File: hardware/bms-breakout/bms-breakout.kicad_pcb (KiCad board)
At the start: 2 copper layers, 150.2 x 100 mm, 26 parts, among them J1 IN-A, J10 V-SUPP, J11 Smol_Brain_Board, J13 UART_CONN, J16 ESTOP_CON, J17 I2C_Conn, J18 BAL_3, J19 BAL_2, J2 IN-B, J20 BAL_1, J21 DE9_Socket_MountingHoles, J22 DE9_Socket_MountingHoles, J23 FAN-IN, J24 SWITCH, J3 IN-C, J4 BALANCE-A, J5 BALANCE-B, J6 BALANCE-C, J7 Conn_01x02, J8 BMS-OUT, J9 BMS-IN, Q1 PMOZZ, SW1 SW_DIP_x02

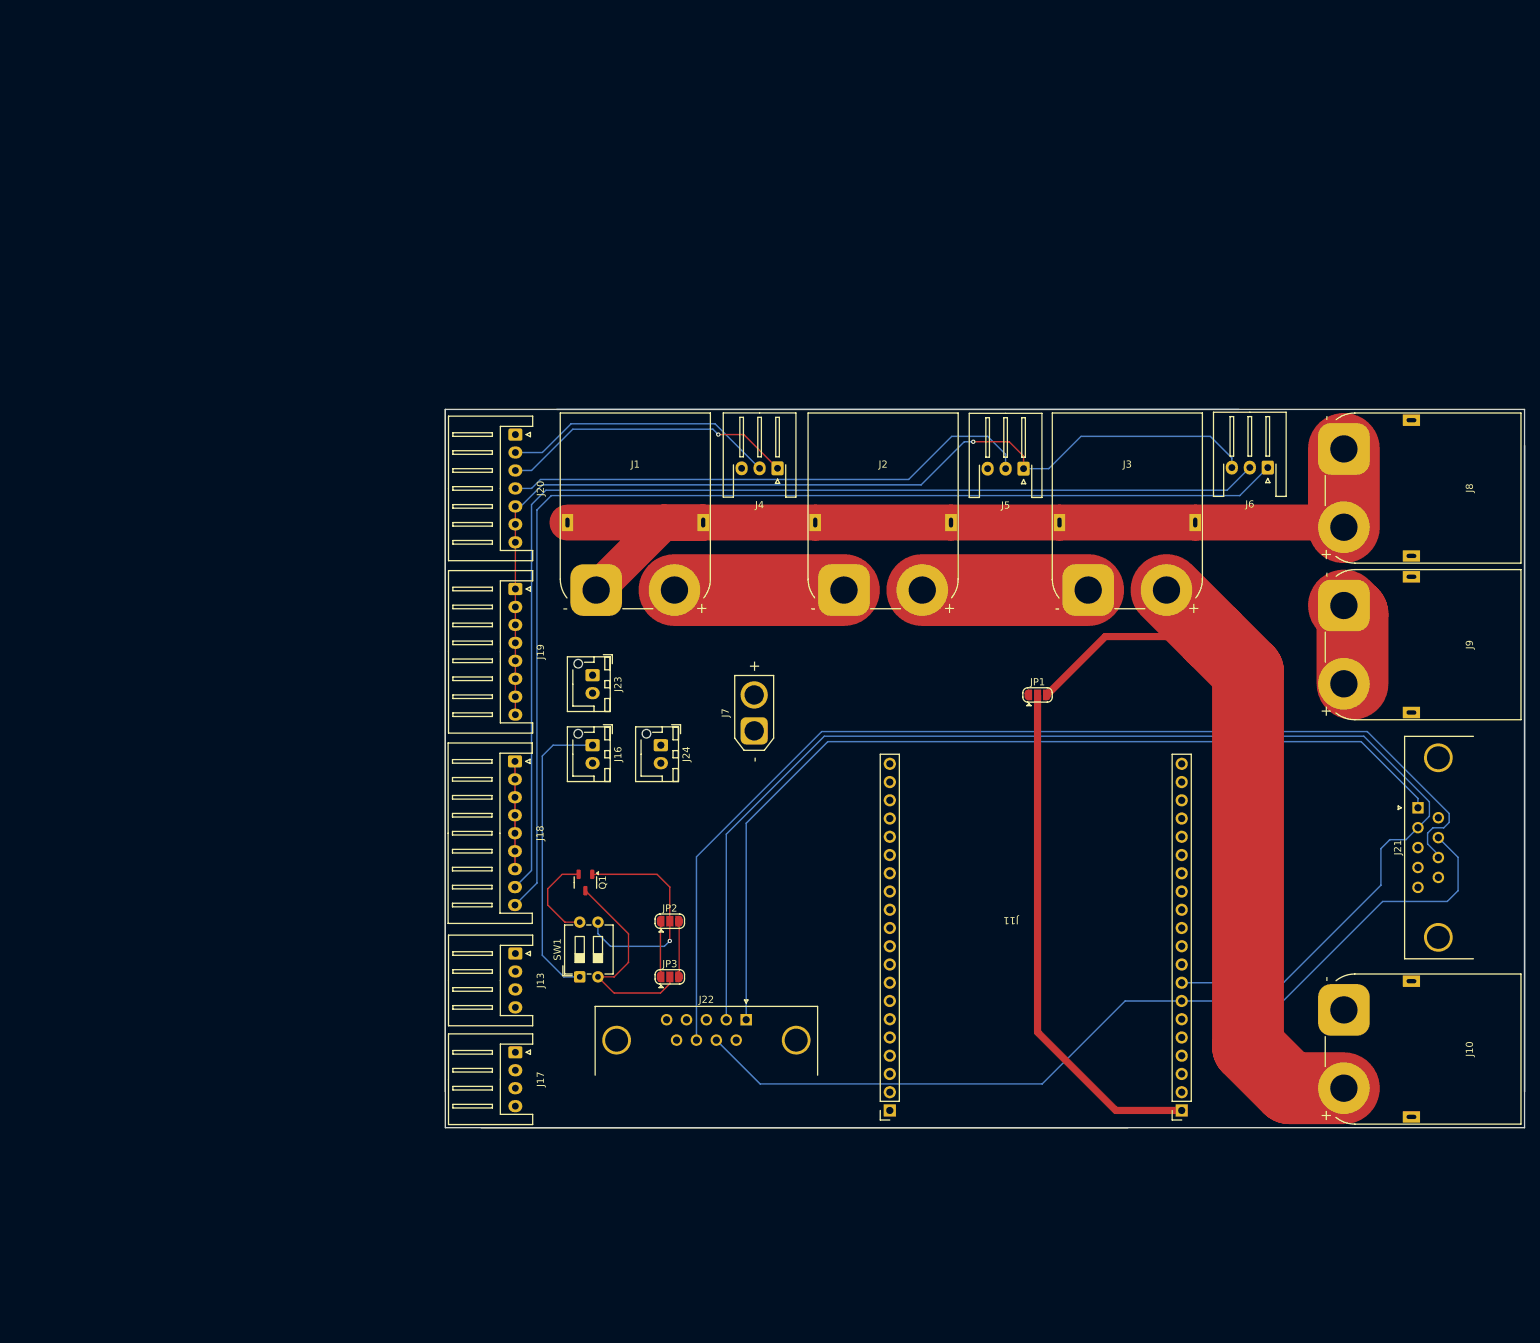
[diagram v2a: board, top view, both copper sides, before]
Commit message: Redid layout
- Redid layout
- Currently tracing board
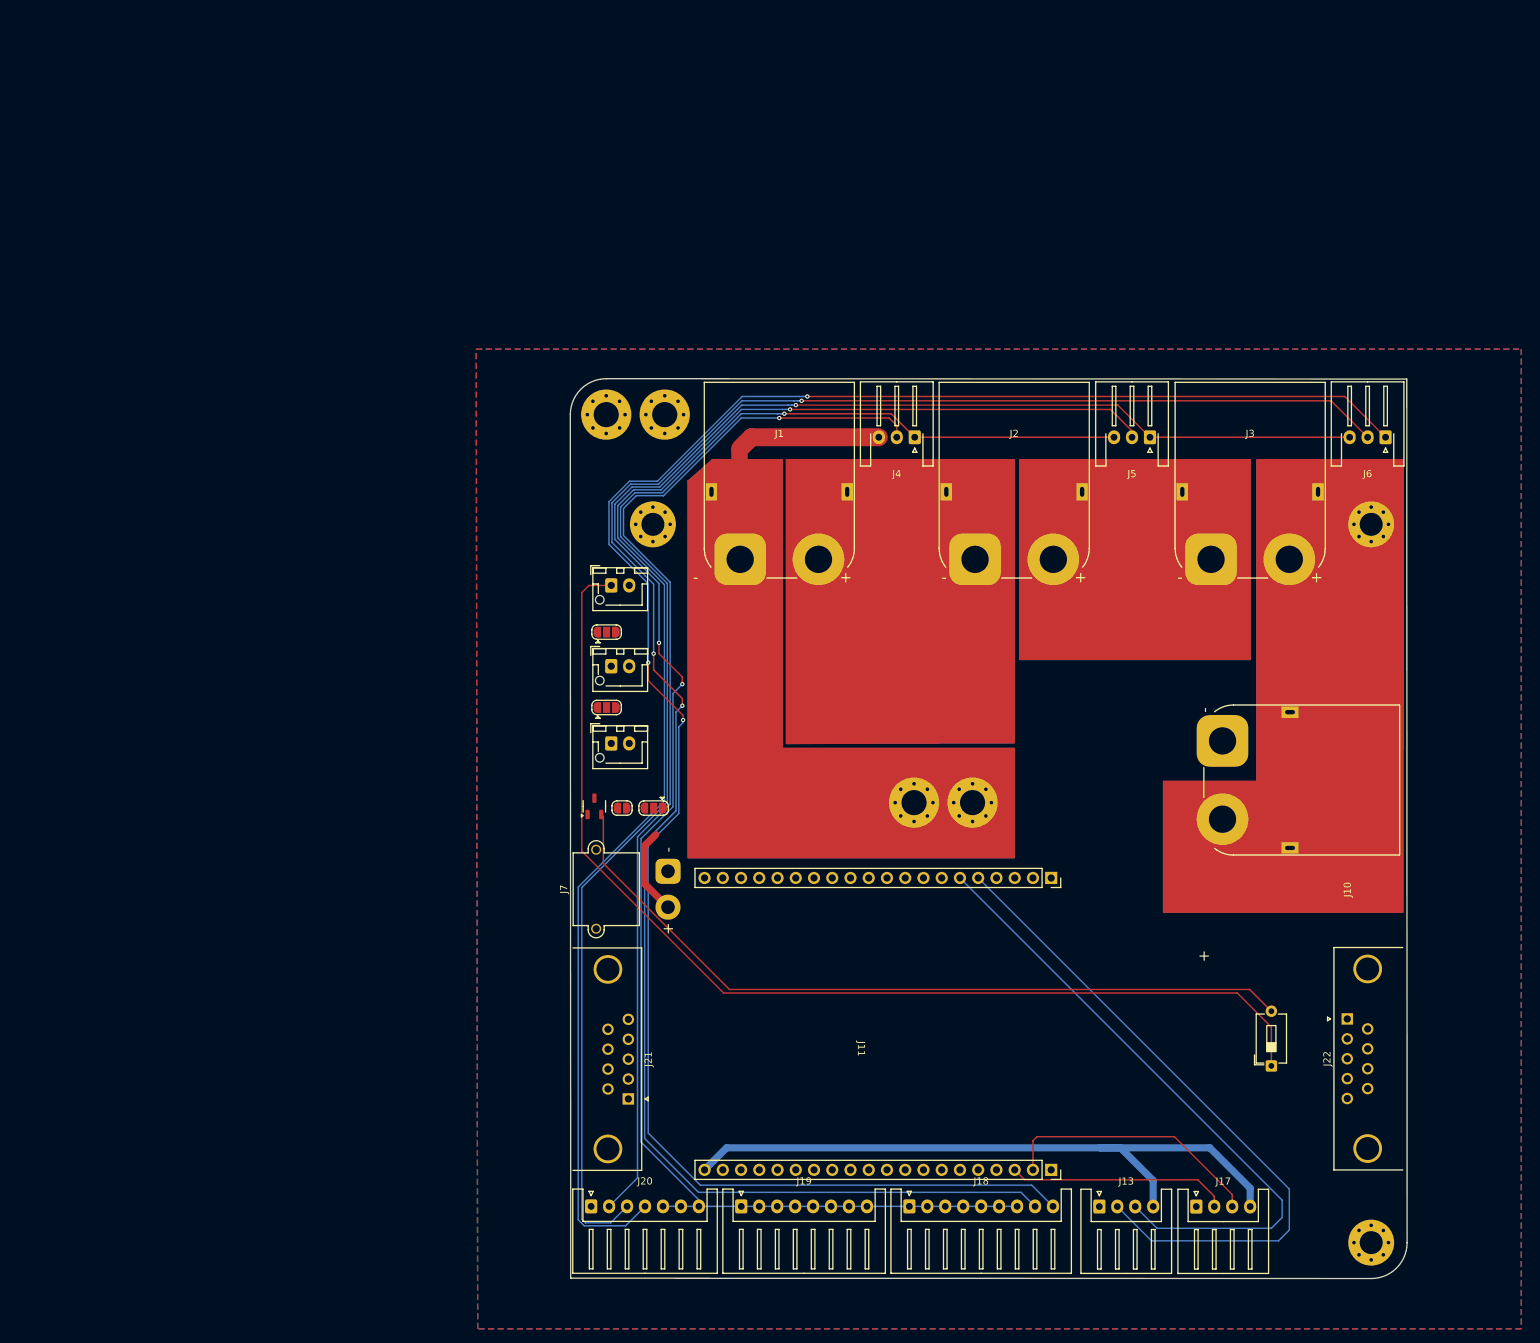
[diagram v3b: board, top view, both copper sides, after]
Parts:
- removed J8: BMS-OUT, Connector_AMASS:AMASS_XT90PW-M_1x02_P10.90mm_Horizontal
- removed J9: BMS-IN, Connector_AMASS:AMASS_XT90PW-M_1x02_P10.90mm_Horizontal
- removed SW1: SW_DIP_x02, Button_Switch_THT:SW_DIP_SPSTx02_Slide_6.7x6.64mm_W7.62mm_P2.54mm_LowProfile
- added H1: Mounting_1, MountingHole:MountingHole_3.2mm_M3_Pad_Via, F.Cu at (78.9, 61.0)
- added H2: Mounting_2, MountingHole:MountingHole_3.2mm_M3_Pad_Via, F.Cu at (178.9, 161.0)
- added H3: Mounting_3, MountingHole:MountingHole_3.2mm_M3_Pad_Via, F.Cu at (178.9, 61.0)
- added H5: BMS_OUT, MountingHole:MountingHole_3.5mm_Pad_Via, F.Cu at (72.4, 45.7)
- added H6: BMS_OUT, MountingHole:MountingHole_3.5mm_Pad_Via, F.Cu at (80.5, 45.7)
- added H7: BMS_IN, MountingHole:MountingHole_3.5mm_Pad_Via, F.Cu at (115.3, 99.7)
- added H8: BMS_IN, MountingHole:MountingHole_3.5mm_Pad_Via, F.Cu at (123.4, 99.7)
- added JP4: Mozz_Jumper, Jumper:SolderJumper-2_P1.3mm_Open_RoundedPad1.0x1.5mm, F.Cu at (74.6, 100.5)
- added SW2: Kill_Switch, Button_Switch_THT:SW_DIP_SPSTx01_Slide_6.7x4.1mm_W7.62mm_P2.54mm_LowProfile, F.Cu at (165.0, 136.4)
- J7: footprint Connector_AMASS:AMASS_XT30U-M_1x02_P5.0mm_Vertical -> Connector_AMASS:AMASS_XT30PW-M_1x02_P2.50mm_Horizontal
- moved J21 117.2 mm to (75.5, 141.0), turned to -90 degrees
- moved J20 108.0 mm to (70.3, 156.0), turned to 0 degrees
- moved J17 97.2 mm to (154.6, 156.0), turned to 0 degrees
- moved J19 91.5 mm to (91.2, 156.0), turned to 0 degrees
- moved J13 88.6 mm to (141.1, 156.0), turned to 0 degrees
- moved J22 83.7 mm to (175.6, 129.9), turned to 90 degrees
- moved J18 82.8 mm to (114.6, 156.0), turned to 0 degrees
- moved JP1 55.7 mm to (79.0, 100.5), turned to 180 degrees
- moved JP2 41.2 mm to (72.5, 76.0)
- moved J10 41.1 mm to (158.2, 91.2)
- moved JP3 38.5 mm to (72.5, 86.5)
- moved J11 28.2 mm to (107.4, 134.0), turned to -90 degrees
- moved J7 22.9 mm to (81.0, 109.3)
- moved J16 22.4 mm to (73.1, 69.5), turned to 0 degrees
- moved J1 20.5 mm to (91.0, 65.9)
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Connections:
- net Net-(J1-Pin_2) renamed /BAT1-2
- net Net-(J2-Pin_2) renamed /BAT2-3
- J1 pad MP: GND_B -> unconnected-(J1-MountPin-PadMP)
- J10 pad MP: GND_C -> unconnected-(J10-MountPin-PadMP)_1
- J2 pad MP: GND_B -> unconnected-(J2-MountPin-PadMP)
- J24 pad 1: /K+ -> /K_NEG
- J24 pad 2: /K+ -> /K_POS
- J3 pad MP: GND_B -> unconnected-(J3-MountPin-PadMP)
- JP2 pad 1: /K+ -> /K_NEG
- JP2 pad 3: /K+ -> /K_POS
- JP3 pad 1: /K+ -> /K_NEG
- JP3 pad 3: /K+ -> /K_POS
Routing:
- net /CAN_L_A: track 182.4 -> 0.00 mm
- net /CAN_H_B: track 151.1 -> 0.00 mm
- net /BAL_2: track 41.1 -> 189.7 mm
- net /CAN_L_B: track 130.2 -> 0.00 mm
- net /CAN_H_A: track 125.5 -> 0.00 mm
- net /BAL_3: track 74.3 -> 197.1 mm, vias 0 -> 1
- net GND_B: track 138.1 -> 20.0 mm
- net /BAL_4: track 154.5 -> 266.5 mm, vias 1 -> 3
- net /BAL_6: track 160.5 -> 271.3 mm, vias 0 -> 3
- net VBUS: track 110.5 -> 0.00 mm
- net /BAL_1: track 38.2 -> 148.7 mm, vias 0 -> 1
- net Net-(J16-Pin_1): track 41.8 -> 152.0 mm
- net /BAL_5: track 156.3 -> 266.2 mm, vias 0 -> 3
- net Net-(Q1-G): track 12.8 -> 108.4 mm
- net +3V3: track 0.00 -> 95.0 mm
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- added copper zone on B.Cu, net GND_C
- added copper zone on F.Cu, net GND_C
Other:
- board size 150.2 x 100 mm -> 116.5 x 125.3 mm

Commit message: Almost finished tracing BMS
- Updated GND planes
- CAN Traces almost done
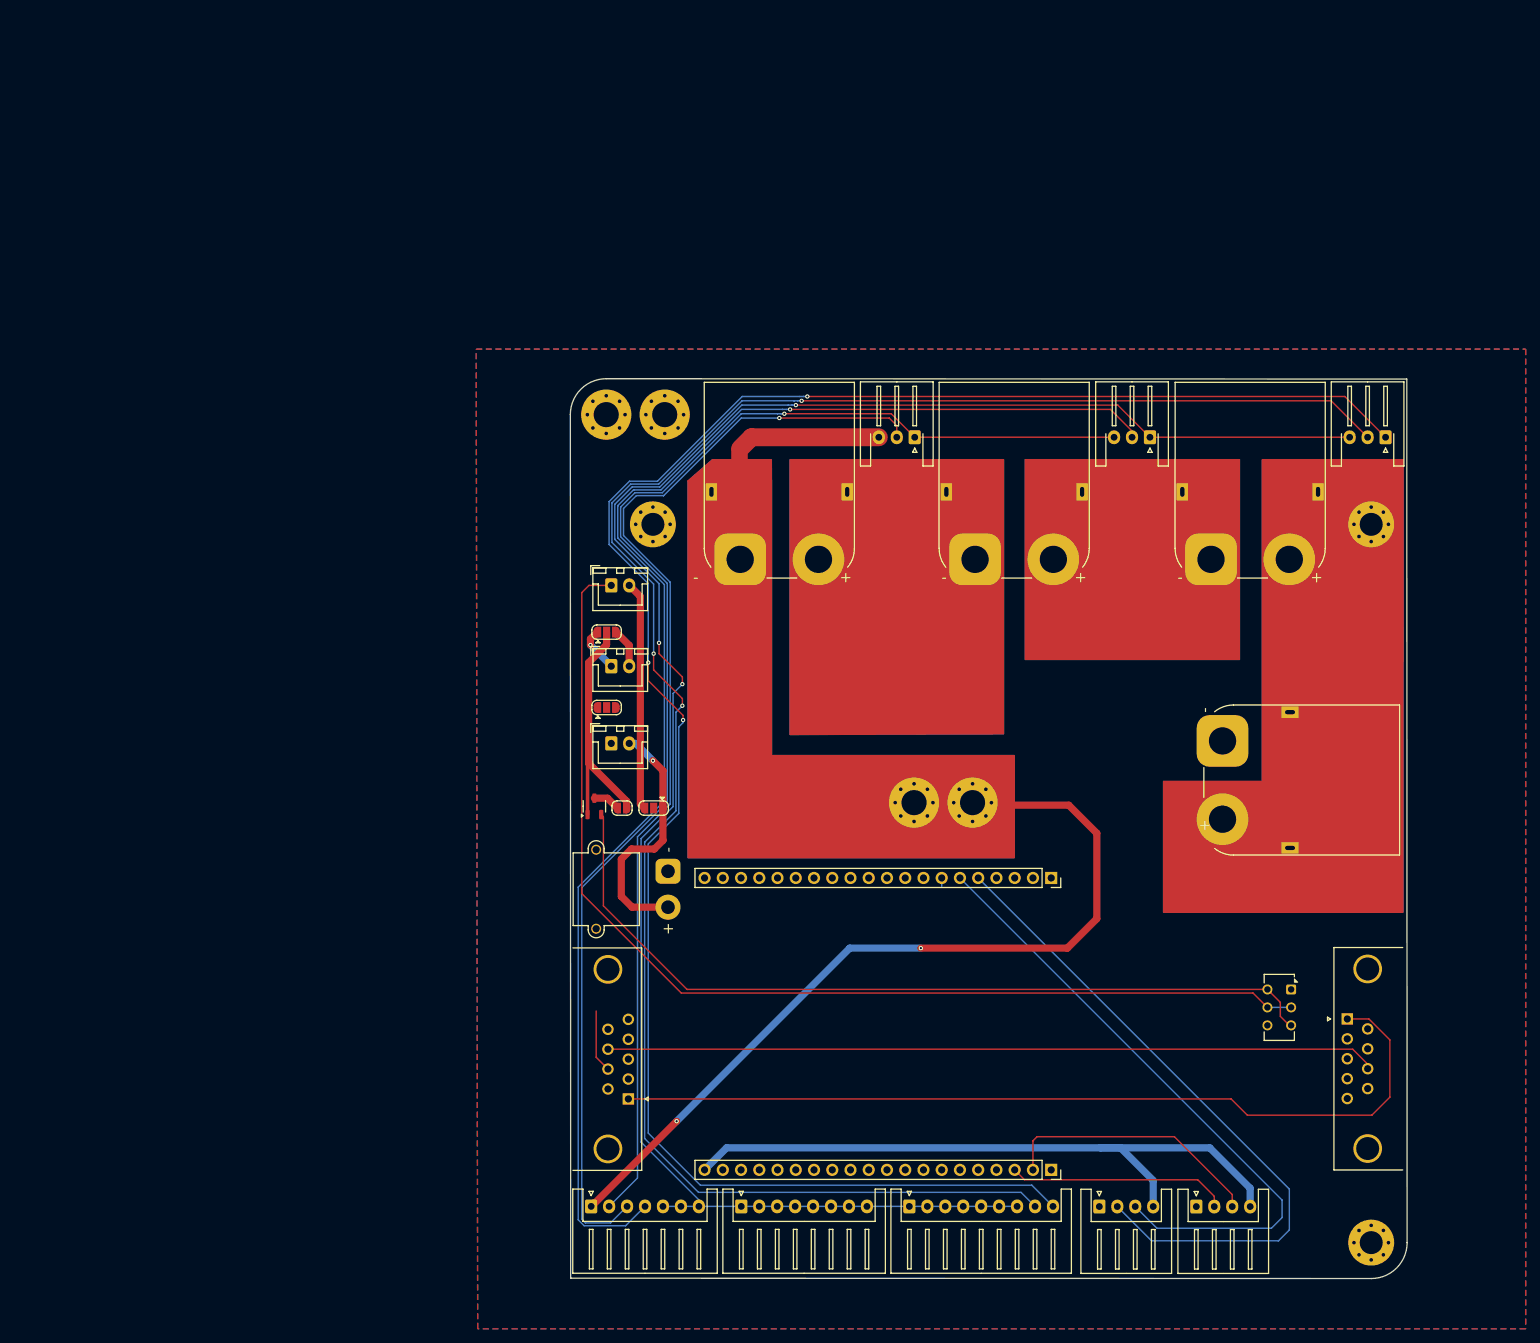
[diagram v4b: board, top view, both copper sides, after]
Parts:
- removed SW2: Kill_Switch, Button_Switch_THT:SW_DIP_SPSTx01_Slide_6.7x4.1mm_W7.62mm_P2.54mm_LowProfile
- added SW1: Kill_Switch, Button_Switch_THT:SW_CK_JS202011CQN_DPDT_Straight, F.Cu at (167.8, 125.8)
- J16, J23, J24: footprint Connector_JST:JST_XH_B2B-XH-AM_1x02_P2.50mm_Vertical -> Connector_JST:JST_XH_B2B-XH-A_1x02_P2.50mm_Vertical
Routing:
- net /CAN_L_B: track 0.00 -> 123.1 mm
- net GND_B: track 20.0 -> 137.9 mm, vias 0 -> 2
- net /CAN_H_B: track 0.00 -> 107.3 mm
- net Net-(JP2-C): track 0.00 -> 34.9 mm
- net VBUS: track 0.00 -> 31.9 mm
- net VCC: track 12.1 -> 35.2 mm, vias 0 -> 1
- net /CAN_H_A: track 0.00 -> 9.95 mm
- net Net-(Q1-G): track 108.4 -> 116.6 mm
- net /K_NEG: track 0.00 -> 6.34 mm, vias 0 -> 1
- net /K_POS: track 0.00 -> 5.52 mm
- net /MOZZ_S: track 0.00 -> 3.77 mm
